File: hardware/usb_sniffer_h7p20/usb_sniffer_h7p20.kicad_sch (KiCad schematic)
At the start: 93 parts, among them J1 FPGA_JTAG, J4 USB_C_Receptacle_USB2.0_16P, J5 FFC-40P-0.5mm,NC, J6 Trigger, U1 H7P20N0L128-M3H1, U6 ZB25VQ16CTJG, U7 CY7C68013A-56LTX, U8 24C32, U9 CJ3439KDW, Y2 24M

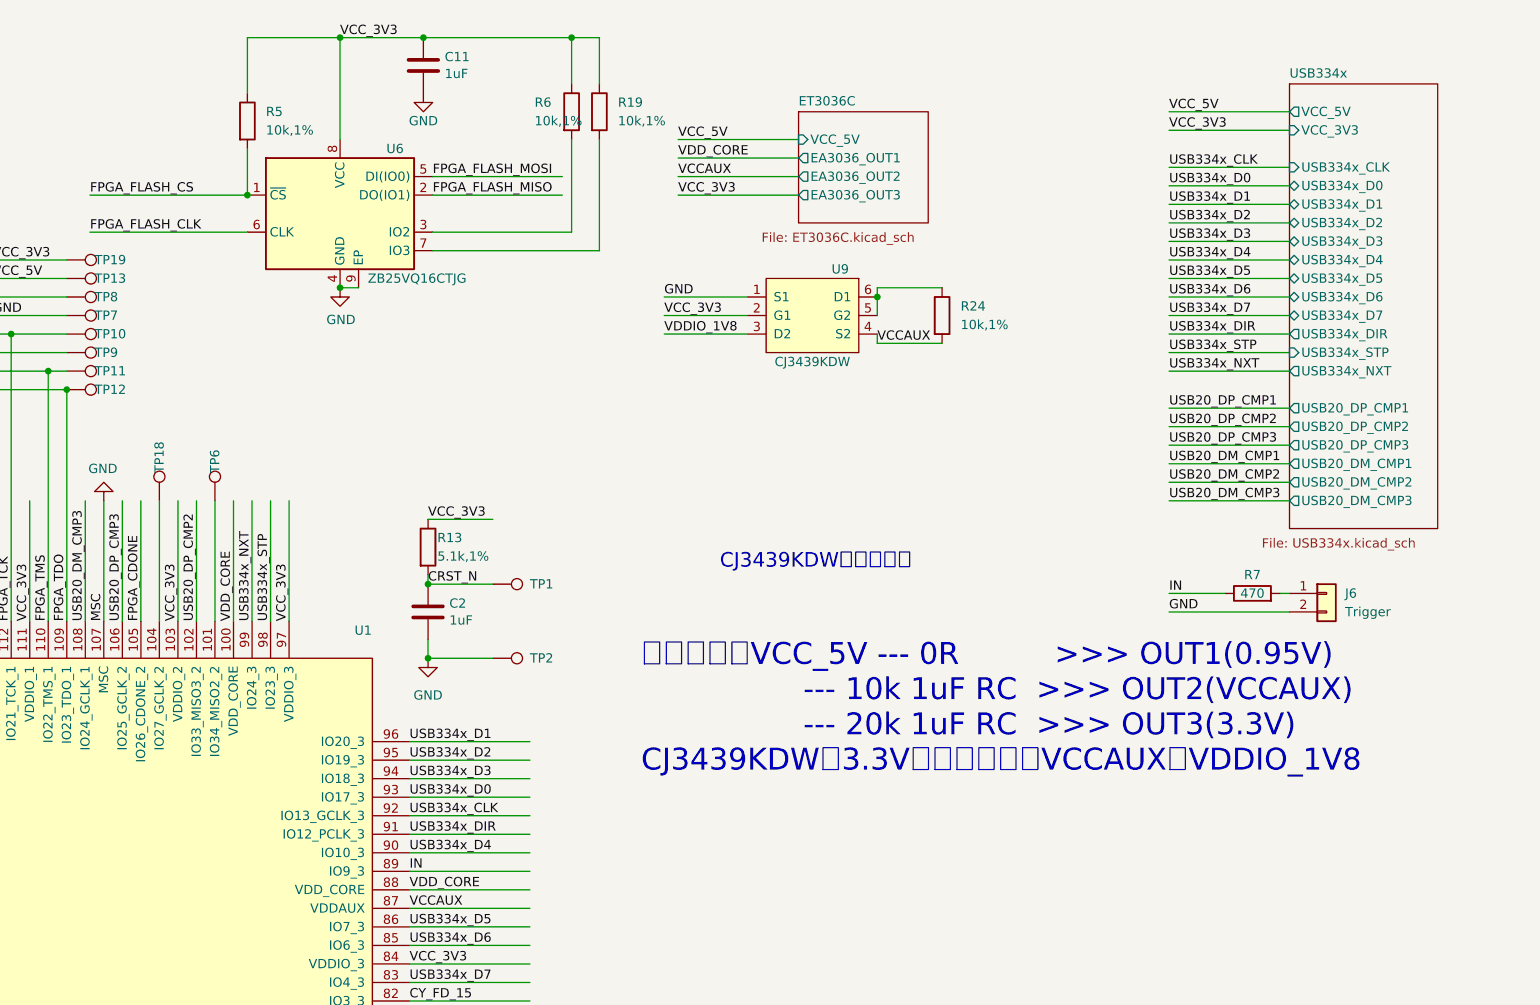
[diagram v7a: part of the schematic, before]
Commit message: [usb_sniffer_h7p20] CH132C测试无数据，回退USB3343
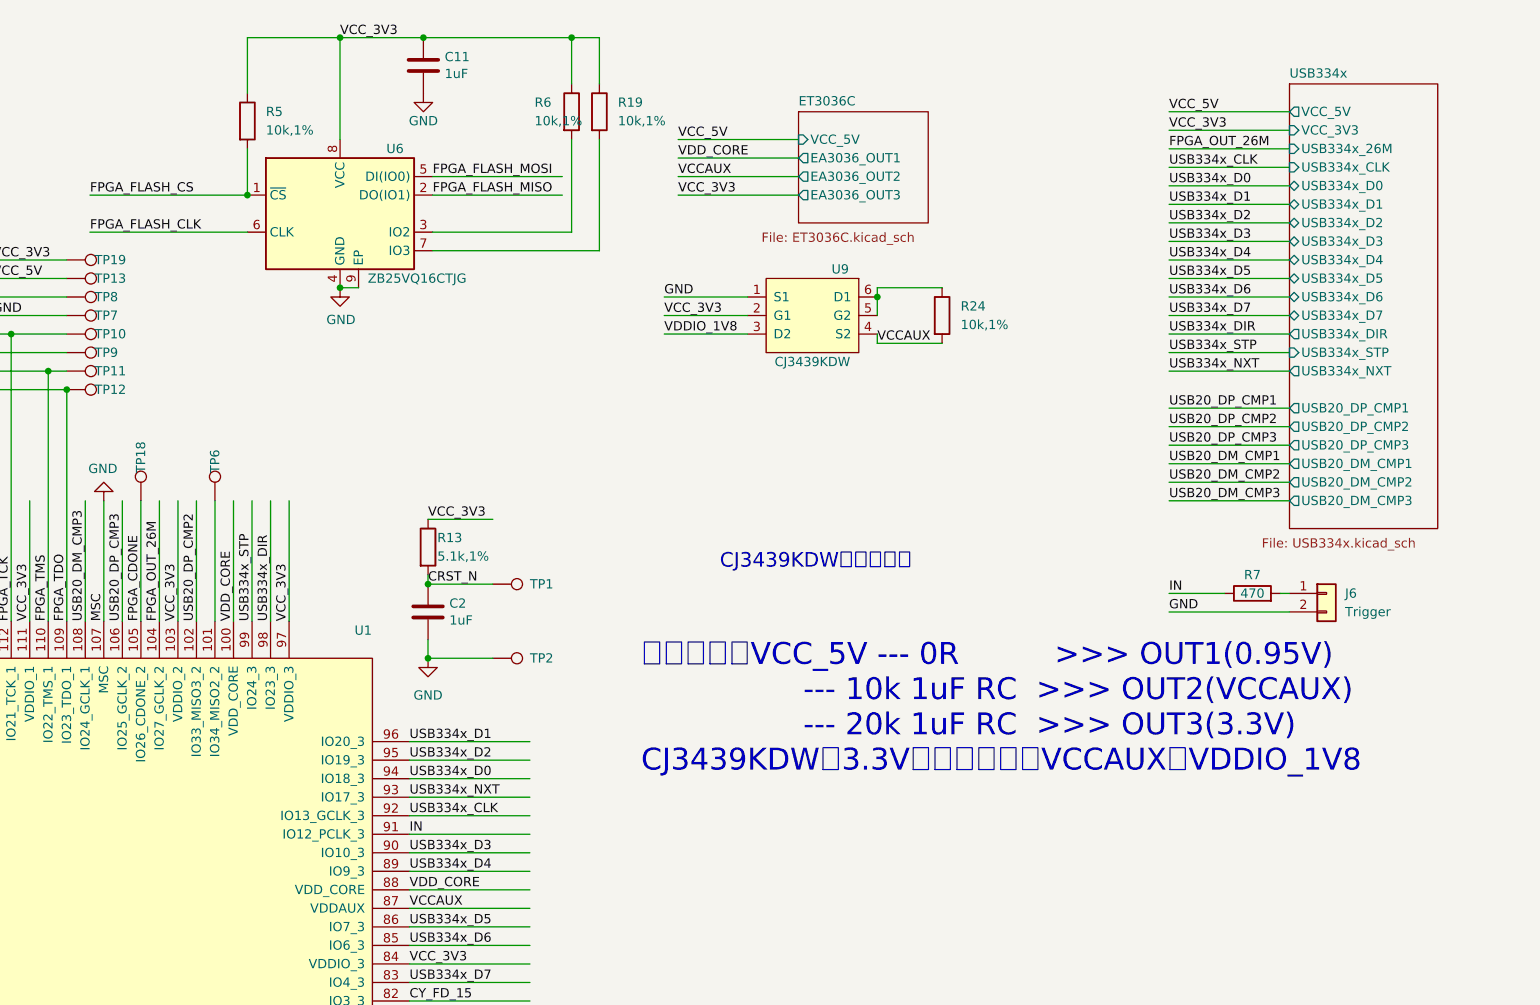
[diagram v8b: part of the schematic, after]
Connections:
- net FPGA_CDONE: now also TP18.1
- net IN: now also U1.91 (IO12_PCLK_3); no longer U1.89 (IO9_3)
- net USB334x_D0: now also U1.94 (IO18_3); no longer U1.93 (IO17_3)
- net USB334x_D3: now also U1.90 (IO10_3); no longer U1.94 (IO18_3)
- net USB334x_D4: now also U1.89 (IO9_3); no longer U1.90 (IO10_3)
- net USB334x_DIR: now also U1.98 (IO23_3); no longer U1.91 (IO12_PCLK_3)
- net USB334x_NXT: now also U1.93 (IO17_3); no longer U1.99 (IO24_3)
- net USB334x_STP: now also U1.99 (IO24_3); no longer U1.98 (IO23_3)
- net FPGA_OUT_26M: now reaches U1.104 (IO27_GCLK_2)
- net FPGA_OUT_26M: no longer TP18.1
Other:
- sheet USB334x ports: added USB334x_26M; removed none
- moved on the sheet: TP18
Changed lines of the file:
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@@
 	(wire
 		(pts
+			(xy 350.52 31.75) (xy 367.03 31.75)
+		)
+		(stroke
+			(width 0)
+			(type default)
+		)
+	)
+	(wire
+		(pts
 			(xy 281.94 223.52) (xy 293.37 223.52)
 		)
@@
 		)
 	)
+	(label "FPGA_OUT_26M"
+		(at 350.52 31.75 0)
+		(effects
+			(font
+				(size 1.27 1.27)
+			)
+			(justify left bottom)
+		)
+	)
 	(label "IN"
-		(at 246.38 130.81 0)
+		(at 246.38 125.73 0)
 		(effects
 			(font
@@
 		)
 	)
+	(label "FPGA_OUT_26M"
+		(at 212.09 96.52 90)
+		(effects
+			(font
+				(size 1.27 1.27)
+			)
+			(justify left bottom)
+		)
+	)
 	(label "B10_IO12P"
 		(at 194.31 224.79 90)
@@
 	)
 	(label "USB334x_NXT"
-		(at 224.79 96.52 90)
+		(at 246.38 120.65 0)
 		(effects
 			(font
@@
 	)
 	(label "USB334x_STP"
-		(at 227.33 96.52 90)
+		(at 224.79 96.52 90)
 		(effects
 			(font
@@
 	)
 	(label "USB334x_D3"
-		(at 246.38 118.11 0)
+		(at 246.38 128.27 0)
 		(effects
 			(font
@@
 	)
 	(label "USB334x_DIR"
-		(at 246.38 125.73 0)
+		(at 227.33 96.52 90)
 		(effects
 			(font
@@
 	)
 	(label "USB334x_D4"
-		(at 246.38 128.27 0)
+		(at 246.38 130.81 0)
 		(effects
 			(font
@@
 	)
 	(label "USB334x_D0"
-		(at 246.38 120.65 0)
+		(at 246.38 118.11 0)
 		(effects
 			(font
@@
 	(symbol
 		(lib_id "Connector:TestPoint")
-		(at 212.09 80.01 0)
+		(at 209.55 80.01 0)
 		(unit 1)
 		(exclude_from_sim no)
@@
 		(dnp no)
 		(property "Reference" "TP18"
-			(at 212.09 76.2 90)
+			(at 209.55 76.2 90)
 			(effects
 				(font
@@
 		)
 		(property "Value" "TestPoint"
-			(at 213.36 74.93 90)
+			(at 210.82 74.93 90)
 			(effects
 				(font
@@
 		)
 		(property "Footprint" "vllogic:TestPoint_Pad_D0.3mm"
-			(at 217.17 80.01 0)
+			(at 214.63 80.01 0)
 			(effects
 				(font
@@
 		)
 		(property "Datasheet" "~"
-			(at 217.17 80.01 0)
+			(at 214.63 80.01 0)
 			(effects
 				(font
@@
 		)
 		(property "Description" ""
-			(at 212.09 80.01 0)
+			(at 209.55 80.01 0)
 			(effects
 				(font
@@
 			(effects
 				(font
+					(size 1.27 1.27)
+				)
+				(justify left)
+			)
+		)
+		(pin "USB334x_26M" input
+			(at 367.03 31.75 180)
+			(effects
+				(font
